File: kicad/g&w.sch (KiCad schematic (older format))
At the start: 193 parts, among them IC1 NAU8315-B31V, IC2 MX25U8035FM2, IC3 LD39020DTPU33R, IC4 DA9230-61VZ2, IC5 BQ24072RGT, J1 speaker, J2 SWD PORT, J3 DISPLAY1, J4 DISPLAY2, J5 Battery, J6 USB-C, Q1 PMBT3904, Q2 PMBT3904, Q3 PMBT3904, Q4 SSM6J412TU, Y1 H01717

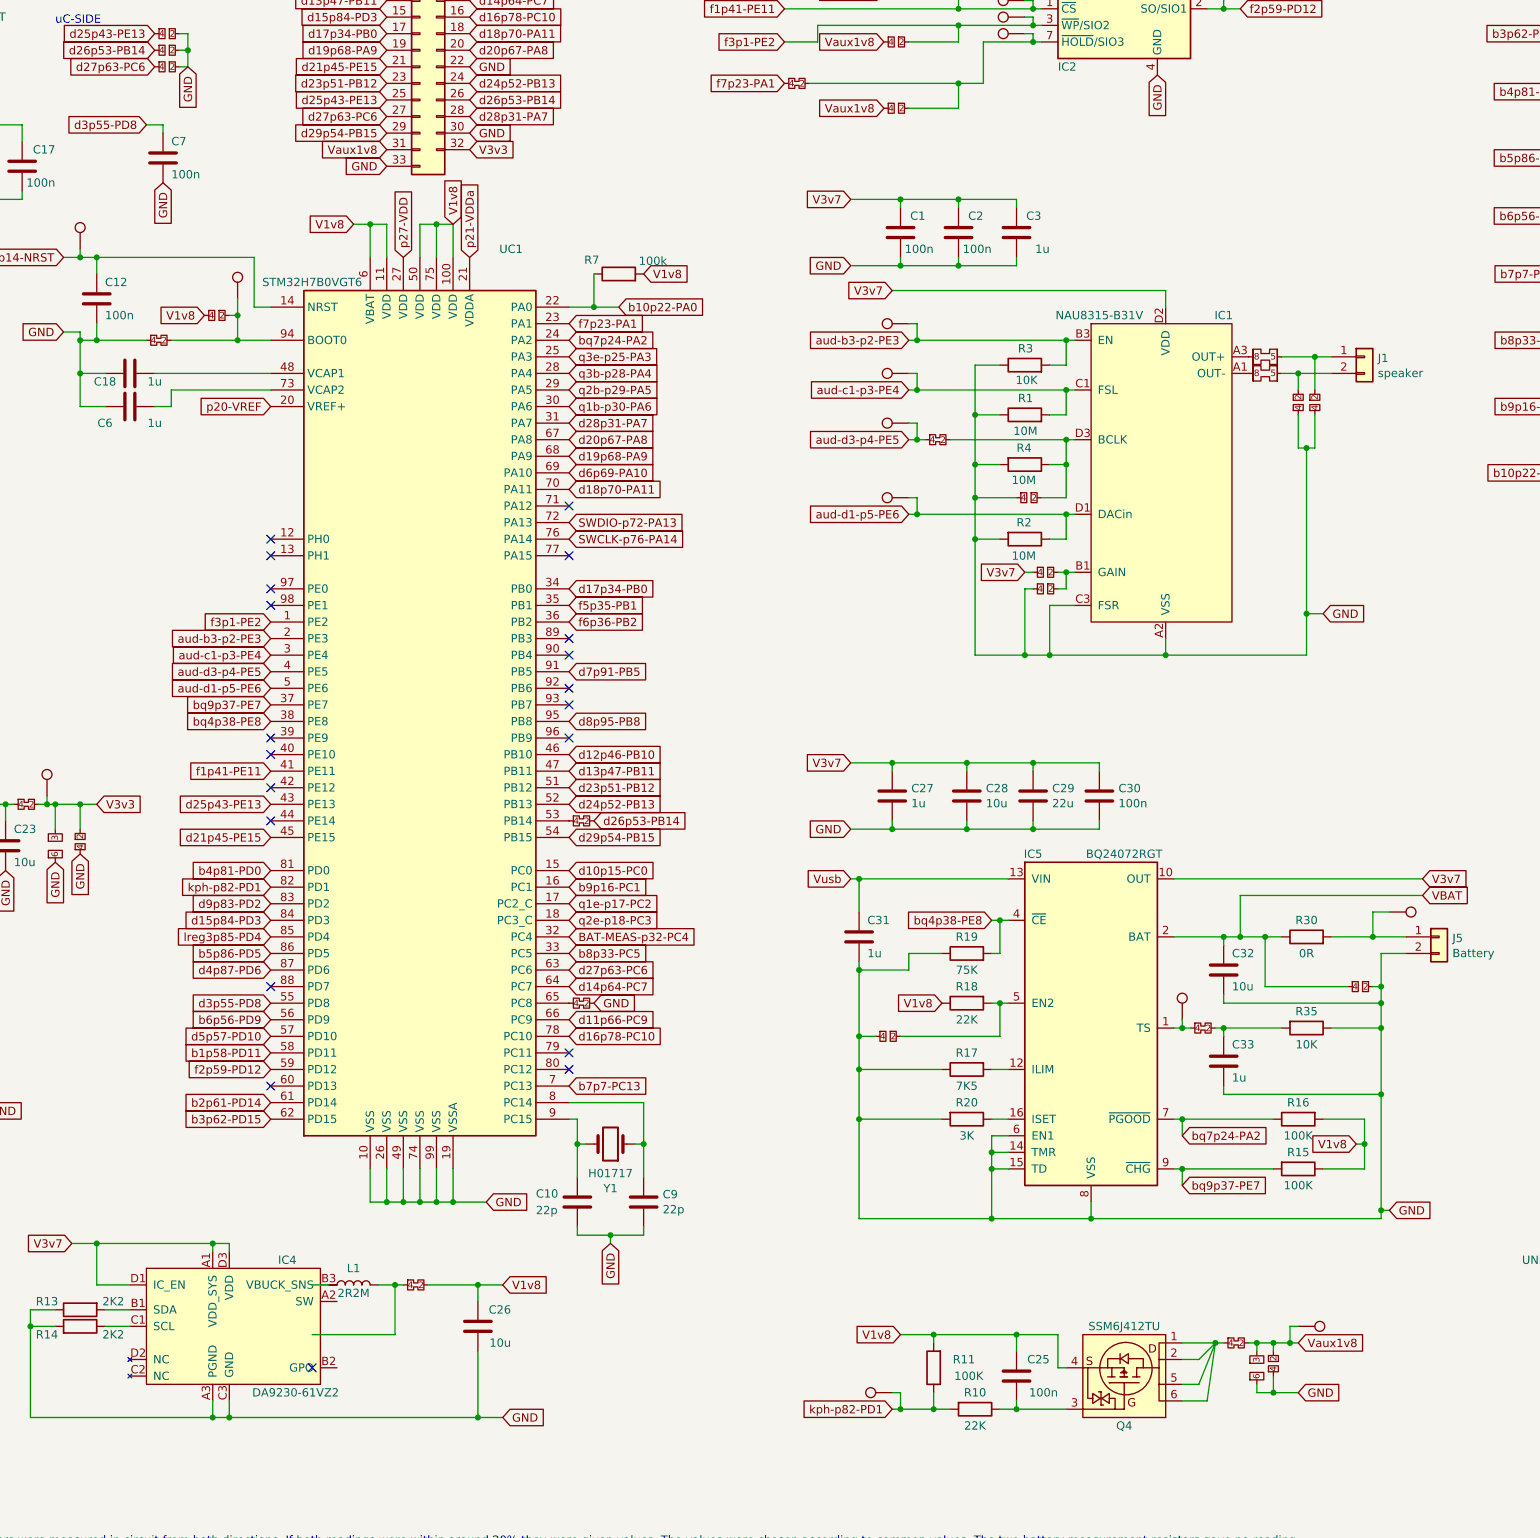
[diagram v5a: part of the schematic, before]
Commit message: all footprints placed, a very rough dxf graphics layer was made to locate most components, several footprints were tweaked and a few missing from the schematic were added and will be in the next revision.
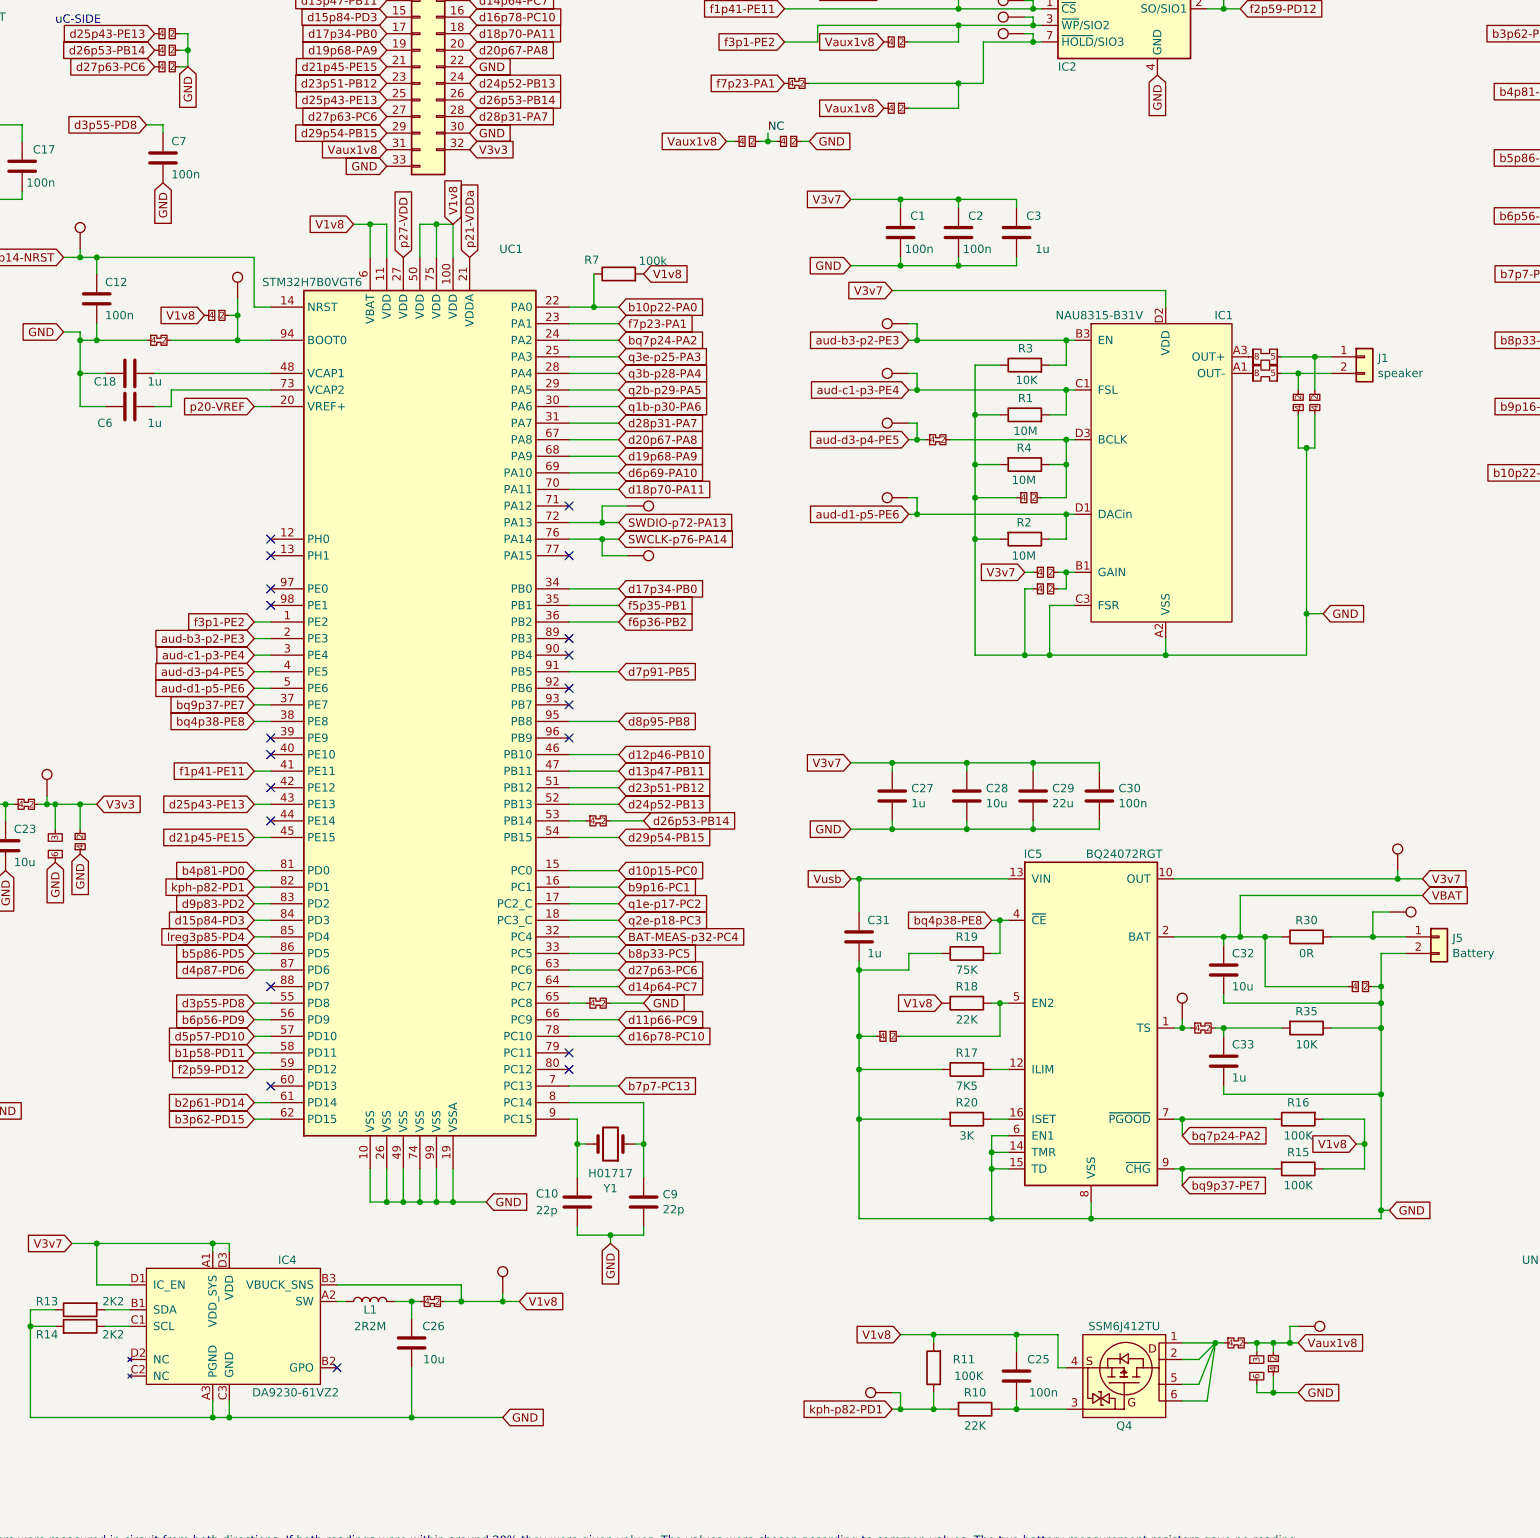
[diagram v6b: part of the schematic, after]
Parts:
- added JP106, JP107: JMP-0402-OPEN, Resistor_SMD:R_0402_1005Metric, symbol gnw_library:JMP-0402-OPEN
- added TP82, TP83, TP84, TP85: TestPoint, gnw:gnw-TestPoint_Pad_D1.0mm, symbol Connector:TestPoint
- L1: footprint Resistor_SMD:R_0402_1005Metric -> gnw:L_0806_2016Metric
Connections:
- net GND: now also JP107.2
- net SWCLK-p76-PA14: now also TP83.1
- net SWDIO-p72-PA13: now also TP82.1
- net V1v8: now also IC4.B3 (VBUCK_SNS), TP84.1; no longer C26.1
- net V3v7: now also TP85.1
- net Vaux1v8: now also JP106.1
- net at IC4.A2 (SW): now also L1.1
- net at JP82.1, L1.2: now also C26.1
- new net NC: JP106.2, JP107.1
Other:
- moved on the sheet: C26, L1

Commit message: about 1/3rd routed
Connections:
- net GND: now also B10.1; no longer B10.2
- net V3v7: no longer JP103.2, JP104.2, JP105.2
- net b10p22-PA0: now also B10.2; no longer B10.1
- net xV3v7: now reaches J4.1 (Pin_1), JP101.2, JP102.2
- net xV3v7: now also JP103.2, JP104.2, JP105.2
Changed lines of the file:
@@
 U 1 1 5FF9AE4E
 P 12650 4350
-F 0 "B10" H 12300 4450 50  0000 C CNN
-F 1 "POWER" H 13000 4450 50  0000 C CNN
+F 0 "B10" H 13000 4450 50  0000 C CNN
+F 1 "POWER" H 12400 4450 50  0000 C CNN
 F 2 "gnw:SW_PUSH_1P1T_Horizontal_Nintendo_GnW" H 12650 4550 50  0001 C CNN
 F 3 "~" H 12650 4550 50  0001 C CNN
 	1    12650 4350
-	1    0    0    -1
+	-1   0    0    -1
 $EndComp
 Text GLabel 13650 2450 2    50   Input ~ 0
@@
 L gnw_library:jmp-0805 JP83
 U 1 1 5FDDC577
-P 10350 3650
-F 0 "JP83" H 10350 3783 50  0001 C CNN
-F 1 "jmp-0805" H 10325 3575 50  0001 C CNN
-F 2 "gnw:JMP-0805-CLOSED" H 10300 3850 50  0001 C CNN
-F 3 "" H 10300 3850 50  0001 C CNN
-	1    10350 3650
+P 10400 3650
+F 0 "JP83" H 10400 3783 50  0001 C CNN
+F 1 "jmp-0805" H 10375 3575 50  0001 C CNN
+F 2 "gnw:JMP-0805-CLOSED" H 10350 3850 50  0001 C CNN
+F 3 "" H 10350 3850 50  0001 C CNN
+	1    10400 3650
 	1    0    0    -1
 $EndComp
@@
 L gnw_library:jmp-0805 JP84
 U 1 1 5FDE4527
-P 10350 3750
-F 0 "JP84" H 10350 3883 50  0001 C CNN
-F 1 "jmp-0805" H 10325 3675 50  0001 C CNN
-F 2 "gnw:JMP-0805-CLOSED" H 10300 3950 50  0001 C CNN
-F 3 "" H 10300 3950 50  0001 C CNN
-	1    10350 3750
+P 10400 3750
+F 0 "JP84" H 10400 3883 50  0001 C CNN
+F 1 "jmp-0805" H 10375 3675 50  0001 C CNN
+F 2 "gnw:JMP-0805-CLOSED" H 10350 3950 50  0001 C CNN
+F 3 "" H 10350 3950 50  0001 C CNN
+	1    10400 3750
 	1    0    0    -1
 $EndComp
@@
 $EndComp
 Wire Wire Line
-	10450 3750 10550 3750
-Wire Wire Line
 	10550 3750 10550 3850
 $Comp
@@
 	10650 3850 10650 3650
 Wire Wire Line
-	10650 3650 10450 3650
+	10650 3650 10500 3650
 Wire Wire Line
 	10650 3650 10750 3650
 Connection ~ 10650 3650
-Connection ~ 10550 3750
 $Comp
 L Device:R R1
@@
 	15400 5750 15400 5850
 Text GLabel 15500 5650 2    50   Input ~ 0
-V3v7
+xV3v7
 Wire Wire Line
 	15500 5650 15400 5650
@@
 Wire Wire Line
 	11150 6800 11300 6800
+Wire Wire Line
+	10300 3650 10250 3650
+Wire Wire Line
+	10250 3750 10300 3750
+Wire Wire Line
+	10500 3750 10550 3750
+Connection ~ 10550 3750
+Text GLabel 15100 4950 2    50   Input ~ 0
+xV3v7
+Wire Wire Line
+	15100 4950 15050 4950
+Wire Wire Line
+	15050 4950 15050 5000
+Connection ~ 15050 5000
 $EndSCHEMATC

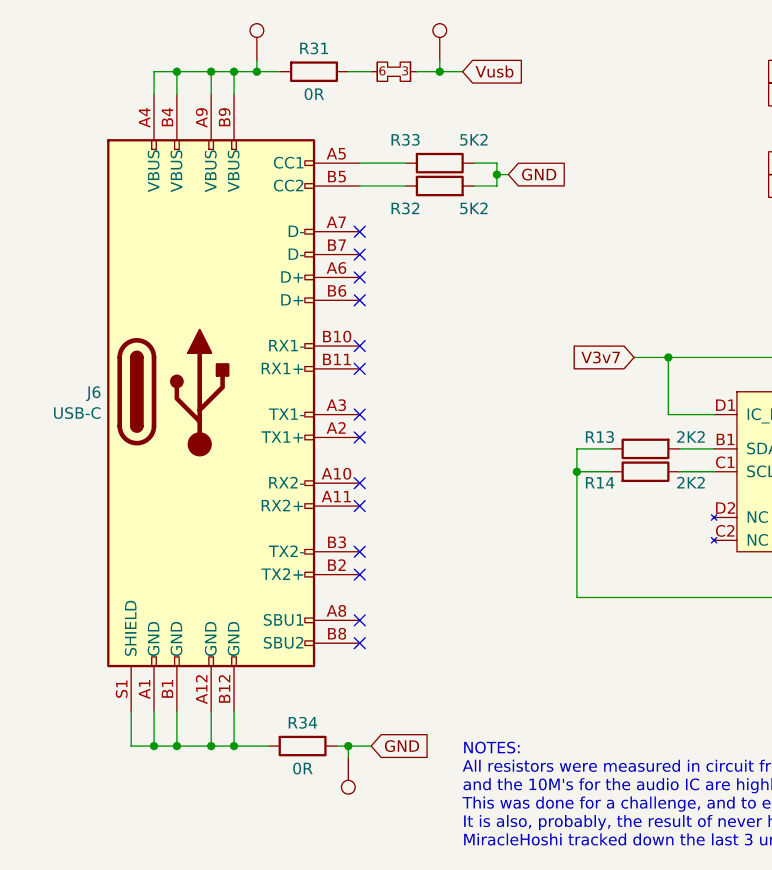
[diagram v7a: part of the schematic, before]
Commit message: first draft: full retrace of interior traces and ground plane. Also the board is designed for 3 layers, No routing conflicts found.
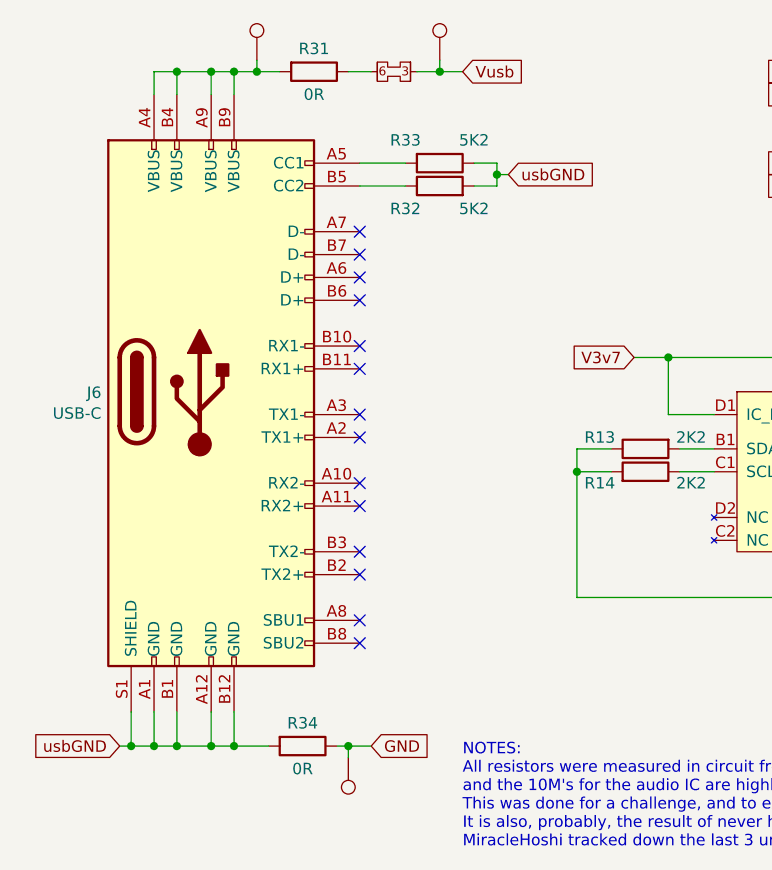
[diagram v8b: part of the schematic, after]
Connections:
- net GND: no longer R32.2, R33.1
- net usbGND: now reaches J6.A1 (GND), J6.A12 (GND), J6.B1 (GND), J6.B12 (GND), J6.S1 (SHIELD), R34.2
- net usbGND: now also R32.2, R33.1
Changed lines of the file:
@@
 $EndComp
 Text GLabel 2600 8200 2    50   Input ~ 0
-GND
+usbGND
 $Comp
 L Device:R R32
@@
 	15050 4950 15050 5000
 Connection ~ 15050 5000
+Text GLabel 900  10700 0    50   Input ~ 0
+usbGND
+Wire Wire Line
+	900  10700 950  10700
+Connection ~ 950  10700
 $EndSCHEMATC
